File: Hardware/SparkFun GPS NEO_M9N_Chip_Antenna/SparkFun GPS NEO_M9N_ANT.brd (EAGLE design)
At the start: 40.6 x 33 mm, 89 parts, among them J2 Qwiic Right Angle, J4 Qwiic Right Angle, U1 U-BLOX_NEO-M9N, U2 3.3V, Y1 GPS_CHIP_ANTENNAW3011

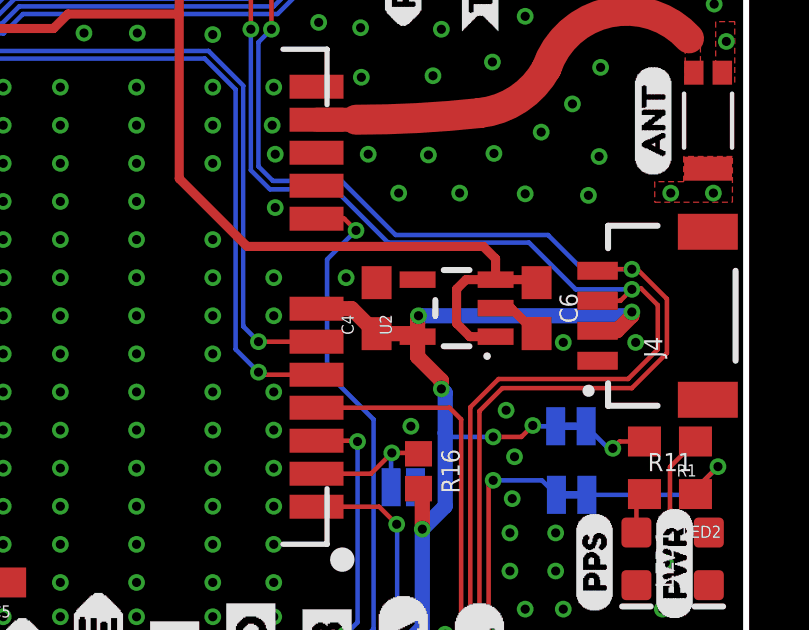
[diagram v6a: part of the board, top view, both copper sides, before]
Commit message: Moves cap by regulator ever so slightly to get cream from module out of keepout
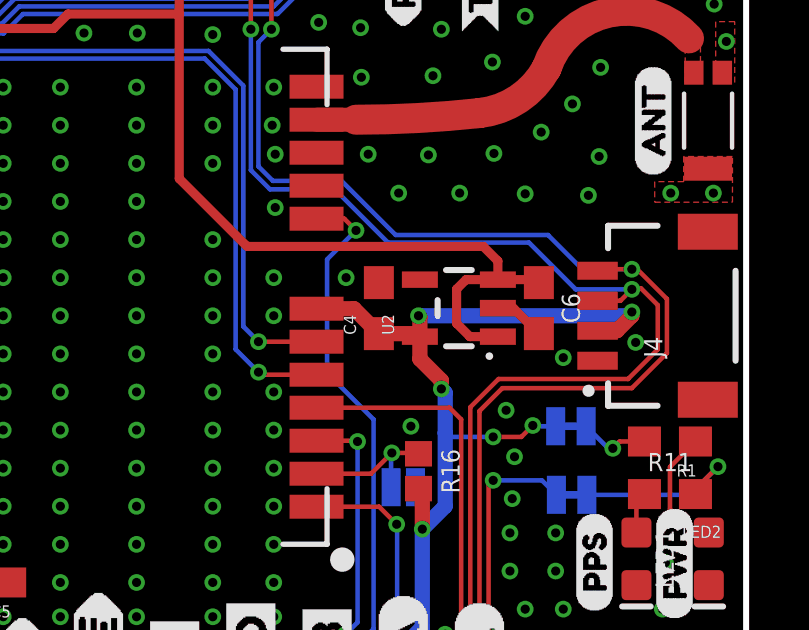
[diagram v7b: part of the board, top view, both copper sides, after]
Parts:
- moved C4 0.08 mm to (28.4, 15.8)
- moved C6 0.08 mm to (33.7, 15.8)
- moved U2 0.08 mm to (31.1, 15.8)

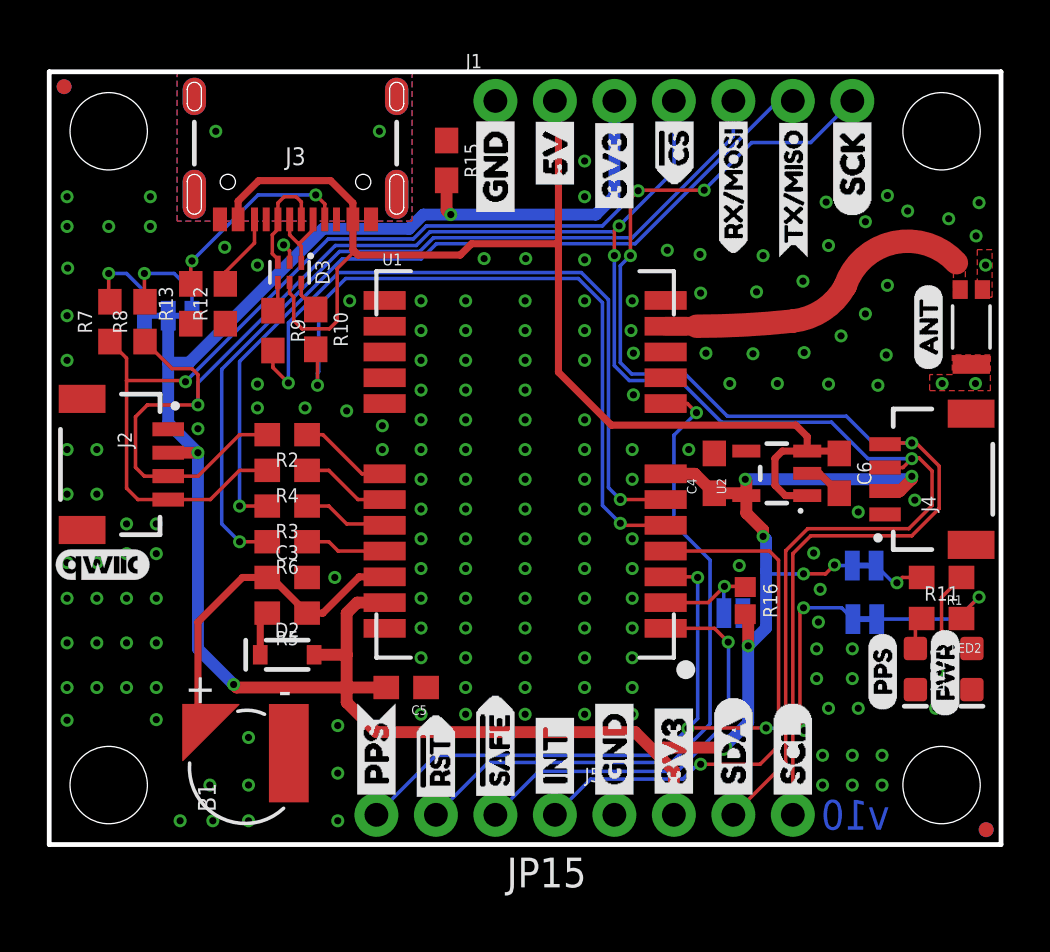
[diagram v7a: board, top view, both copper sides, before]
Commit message: Moves left qwiic connector down to match right one, updates measures, moves some vias
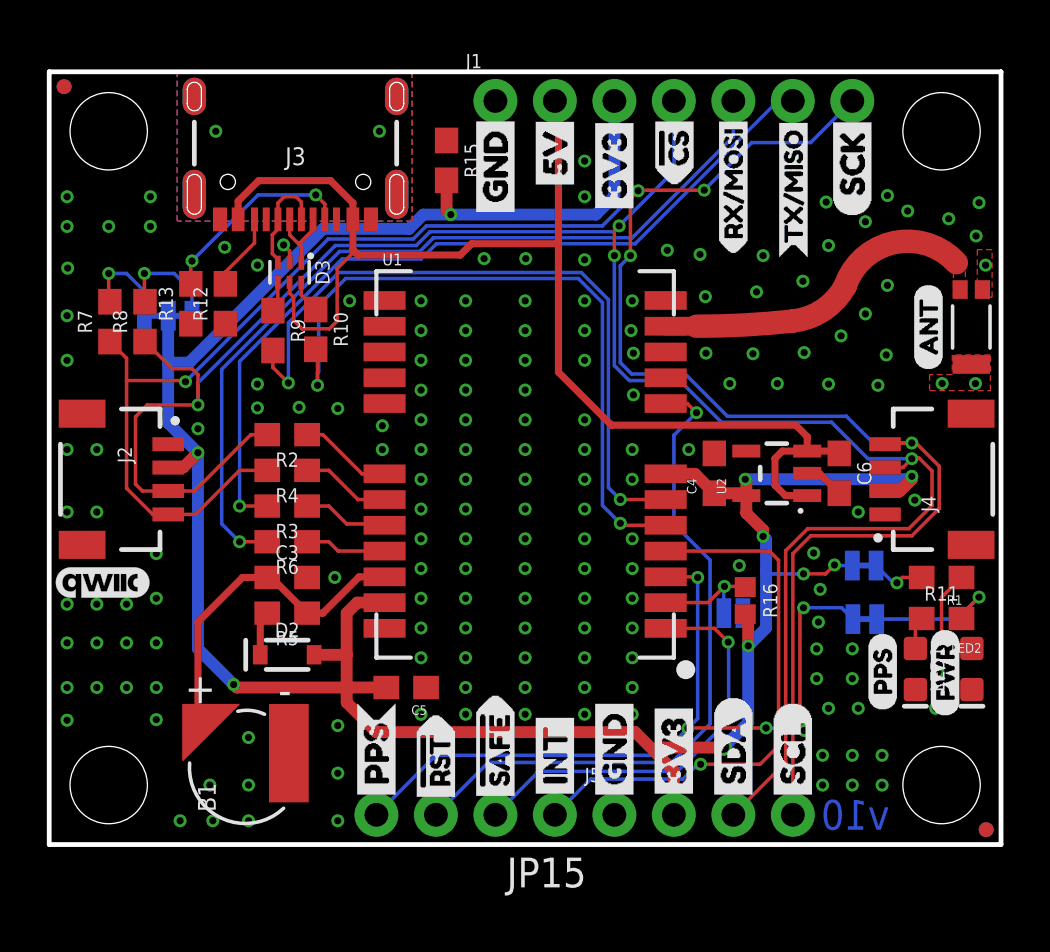
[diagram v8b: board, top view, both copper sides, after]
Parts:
- moved U$14 0.76 mm to (2.29, 11.2)
- moved J2 0.63 mm to (5.08, 15.6)
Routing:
- net SDA/!CS: track 87.2 -> 88.8 mm
- net SCL/SCK: track 93.5 -> 94.1 mm
- net GND: vias 178 -> 173
